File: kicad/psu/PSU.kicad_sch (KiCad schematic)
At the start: 56 parts, among them J1 B2B-PH-K-S, J2 Conn_01x09_Pin, J3 *, U1 BQ21040DBVR, U2 RT4812GJ8F, U3 AP3445LW6-7, U4 AP3445LW6-7

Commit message: Minor PSU changes
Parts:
- added U5: LM66200DRLR, SOT-5X3_DRL_TEX, symbol 2025-12-15_03-55-30:LM66200DRLR
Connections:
- net GND: now also U5.1 (GND), U5.4 (ON), U5.5 (GND)
- net Vcharger: now also U5.2 (VOUT), U5.7 (VOUT); no longer D5.1 (K), J3.A9 (VBUS), J3.B9 (VBUS)
- new net Vcharger_MCU: D5.1 (K), U5.6 (VIN2)
- new net Vcharger_USB: J3.A9 (VBUS), J3.B9 (VBUS), U5.3 (VIN1), U5.8 (ST)

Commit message: PSU Diodes
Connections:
- net 3.3V: now also D4.2 (A)
- net 3.3V_T: no longer D4.2 (A)
- net Vcharger_USB: no longer U5.8 (ST)
- no-connect marks 0 -> 1
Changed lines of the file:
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@@
 		(color 0 0 0 0)
+	)
+	(no_connect
+		(at 154.94 181.61)
 	)
 	(wire
@@
 		)
 	)
-	(global_label "3.3V_T"
+	(global_label "3.3V"
 		(shape input)
 		(at 68.58 31.75 180)
@@
 		)
 		(property "Intersheetrefs" "${INTERSHEET_REFS}"
-			(at 59.5472 31.75 0)
+			(at 61.4824 31.75 0)
 			(effects
 				(font
@@
 				(hide yes)
 			)
-		)
-	)
-	(global_label "Vcharger_USB"
-		(shape input)
-		(at 154.94 181.61 0)
-		(fields_autoplaced yes)
-		(effects
-			(font
-				(size 1.27 1.27)
-			)
-			(justify left)
-		)
-		(property "Intersheetrefs" "${INTERSHEET_REFS}"
-			(at 170.988 181.61 0)
-			(effects
-				(font
-					(size 1.27 1.27)
-				)
-				(justify left)
-				(hide yes)
-			)

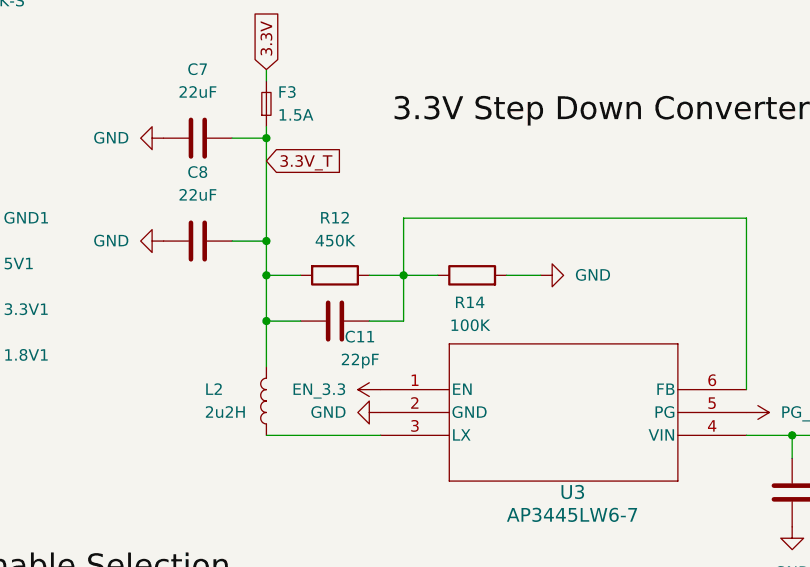
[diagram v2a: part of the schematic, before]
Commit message: Minor PSU Tweaks
removed non existent resistors and updated components
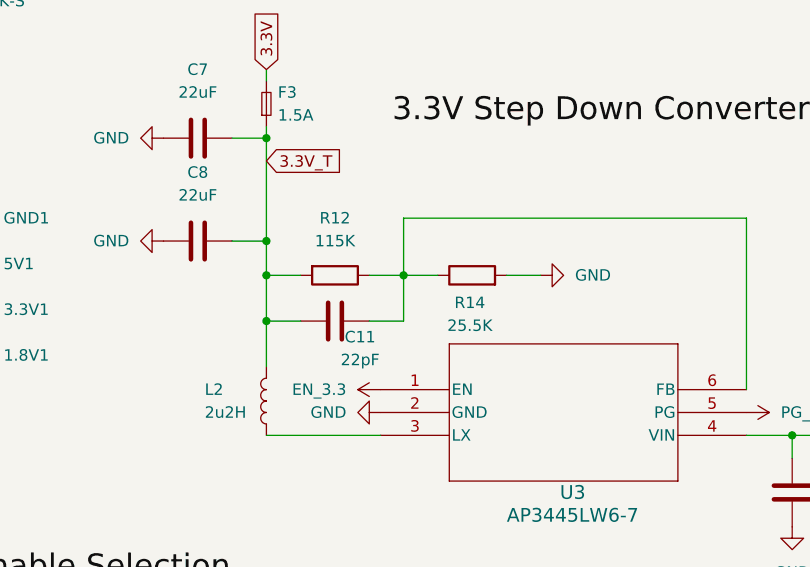
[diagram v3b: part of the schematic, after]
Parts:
- D2, D3, D4, D5, D6: footprint Diode_SMD:D_0805_2012Metric -> Diode_SMD:D_SOD-123
- F2, F3, F4: footprint Fuse:Fuse_0805_2012Metric -> Fuses:0451Series_LTF
- R12: value 450K -> 115K
- R14: value 100K -> 25.5K
- U5: footprint SOT-5X3_DRL_TEX -> footprints:SOT-5X3_DRL_TEX
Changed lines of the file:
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@@
 			)
 		)
-		(property "Value" "450K"
+		(property "Value" "115K"
 			(at 195.58 102.87 90)
 			(effects
@@
 			)
 		)
-		(property "Footprint" "Diode_SMD:D_0805_2012Metric"
+		(property "Footprint" "Diode_SMD:D_SOD-123"
 			(at 72.39 26.67 0)
 			(effects
@@
 			)
 		)
-		(property "Footprint" "Diode_SMD:D_0805_2012Metric"
+		(property "Footprint" "Diode_SMD:D_SOD-123"
 			(at 72.39 31.75 0)
 			(effects
@@
 			)
 		)
-		(property "Footprint" "Diode_SMD:D_0805_2012Metric"
+		(property "Footprint" "Diode_SMD:D_SOD-123"
 			(at 72.39 29.21 0)
 			(effects
@@
 			)
 		)
-		(property "Footprint" "SOT-5X3_DRL_TEX"
+		(property "Footprint" "footprints:SOT-5X3_DRL_TEX"
 			(at 114.3 181.61 0)
 			(effects
@@
 			)
 		)
-		(property "Footprint" "Diode_SMD:D_0805_2012Metric"
+		(property "Footprint" "Diode_SMD:D_SOD-123"
 			(at 71.12 46.99 0)
 			(effects
@@
 			)
 		)
-		(property "Footprint" "Fuse:Fuse_0805_2012Metric"
+		(property "Footprint" "Fuses:0451Series_LTF"
 			(at 190.5 22.86 0)
 			(effects
@@
 			)
 		)
-		(property "Footprint" "Diode_SMD:D_0805_2012Metric"
+		(property "Footprint" "Diode_SMD:D_SOD-123"
 			(at 72.39 34.29 0)
 			(effects
@@
 			)
 		)
-		(property "Value" "100K"
+		(property "Value" "25.5K"
 			(at 210.566 112.268 90)
 			(effects
@@
 			)
 		)
-		(property "Footprint" "Fuse:Fuse_0805_2012Metric"
+		(property "Footprint" "Fuses:0451Series_LTF"
 			(at 127 148.59 0)
 			(effects
@@
 			)
 		)
-		(property "Footprint" "Fuse:Fuse_0805_2012Metric"
+		(property "Footprint" "Fuses:0451Series_LTF"
 			(at 187.96 87.63 0)
 			(effects

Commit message: Update PSU.kicad_sch
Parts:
- R6: value 100K -> 30K
- R7: value 900K -> 270K
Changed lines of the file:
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@@
 			)
 		)
-		(property "Value" "100K"
+		(property "Value" "30K"
 			(at 99.06 154.9399 0)
 			(effects
@@
 			)
 		)
-		(property "Value" "900K"
+		(property "Value" "270K"
 			(at 99.06 165.0999 0)
 			(effects

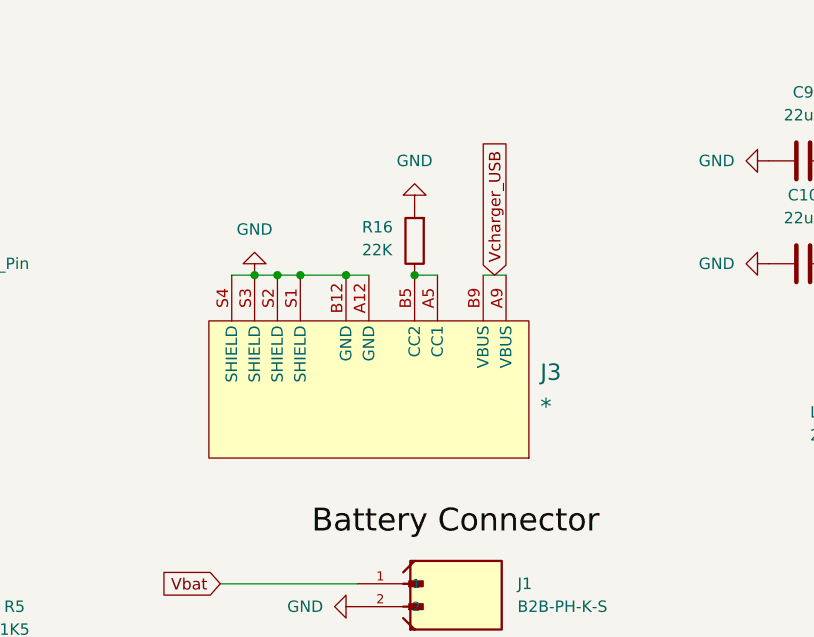
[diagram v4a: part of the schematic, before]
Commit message: new symbols & footprints for connectors and usb-c
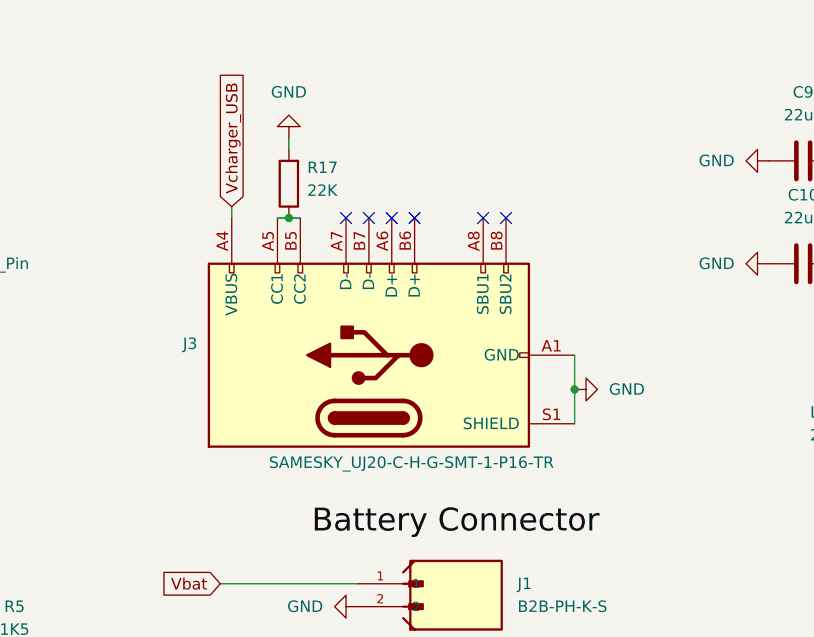
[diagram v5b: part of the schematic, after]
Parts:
- removed J3: *, PSAT_Library:GCT_USB4125-GF-A_REVA2, symbol PSAT_Library:USB4125-GF-A_REVA2
- removed R16: 22K, Resistor_SMD:R_0805_2012Metric, symbol Device:R
- added J3: SAMESKY_UJ20-C-H-G-SMT-1-P16-TR, UJ20_C_H_G_SMT_1_P16_TR:SAMESKY_UJ20-C-H-G-SMT-1-P16-TR, symbol Connector:USB_C_Receptacle_USB2.0_16P
- added R17: 22K, Resistor_SMD:R_0805_2012Metric, symbol Device:R
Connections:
- net GND: now also J3.A1 (GND), J3.A12 (GND), J3.B1 (GND), J3.B12 (GND), J3.S1 (SHIELD), R17.2
- net Vcharger_USB: now also J3.A4 (VBUS), J3.A9 (VBUS), J3.B4 (VBUS), J3.B9 (VBUS)
- new net: J3.A5 (CC1), J3.B5 (CC2), R17.1
- no-connect marks 1 -> 7

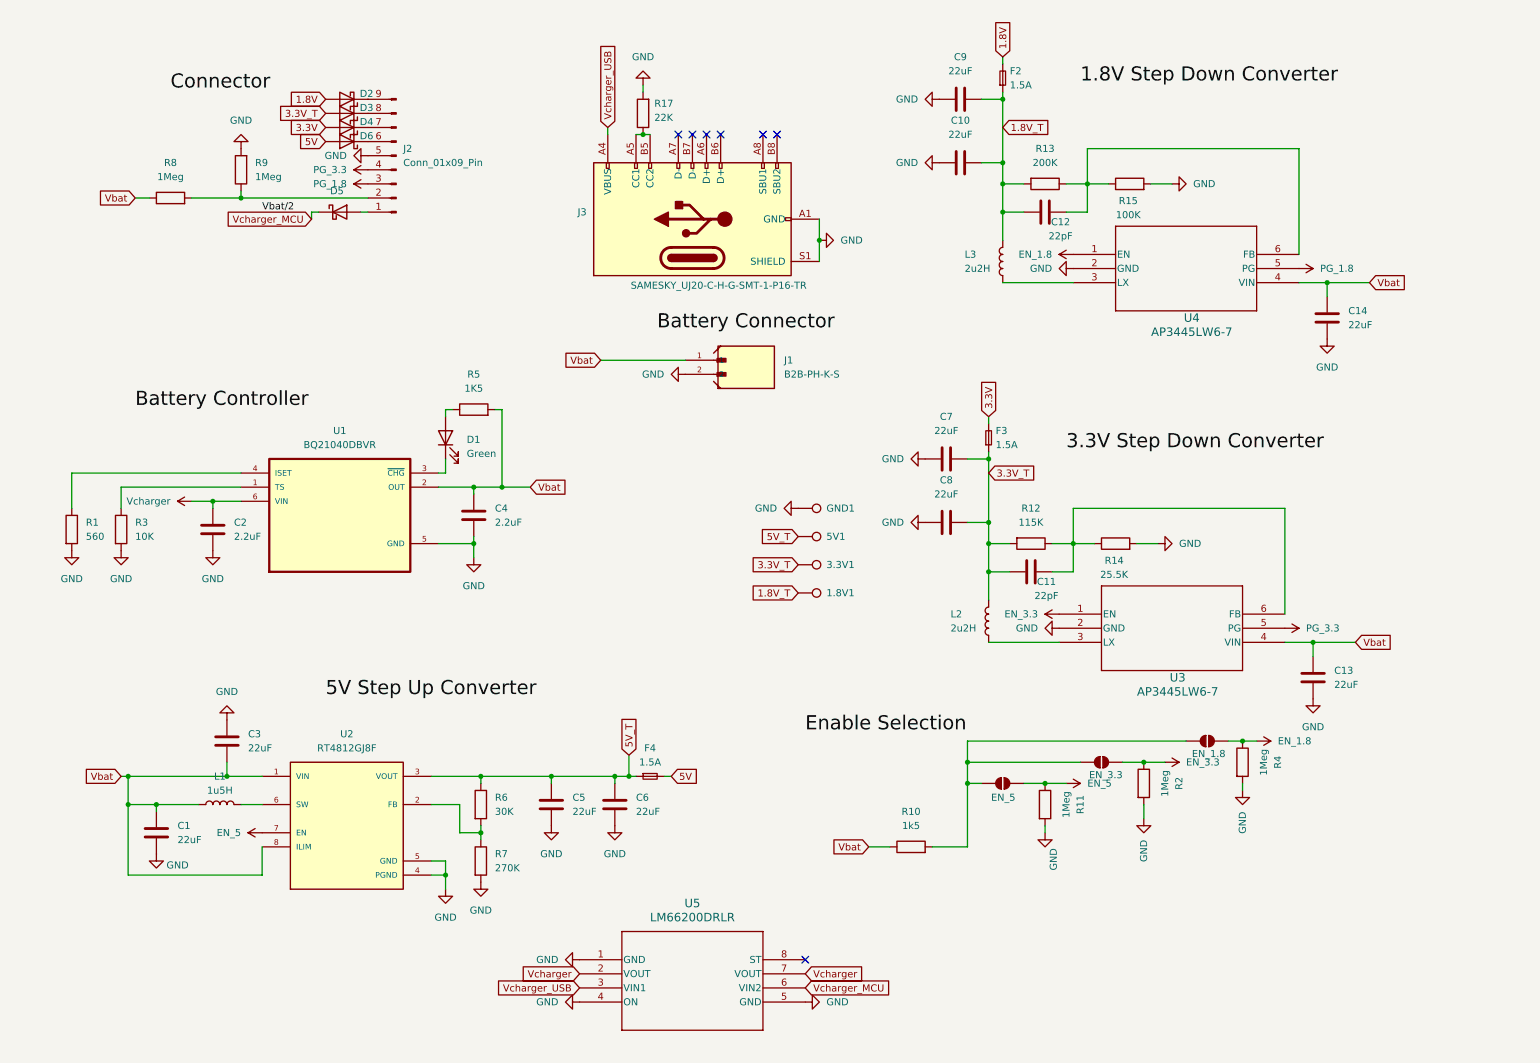
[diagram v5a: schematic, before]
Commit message: Kicad(psu): changed the connector and usb-c to different psu footprints
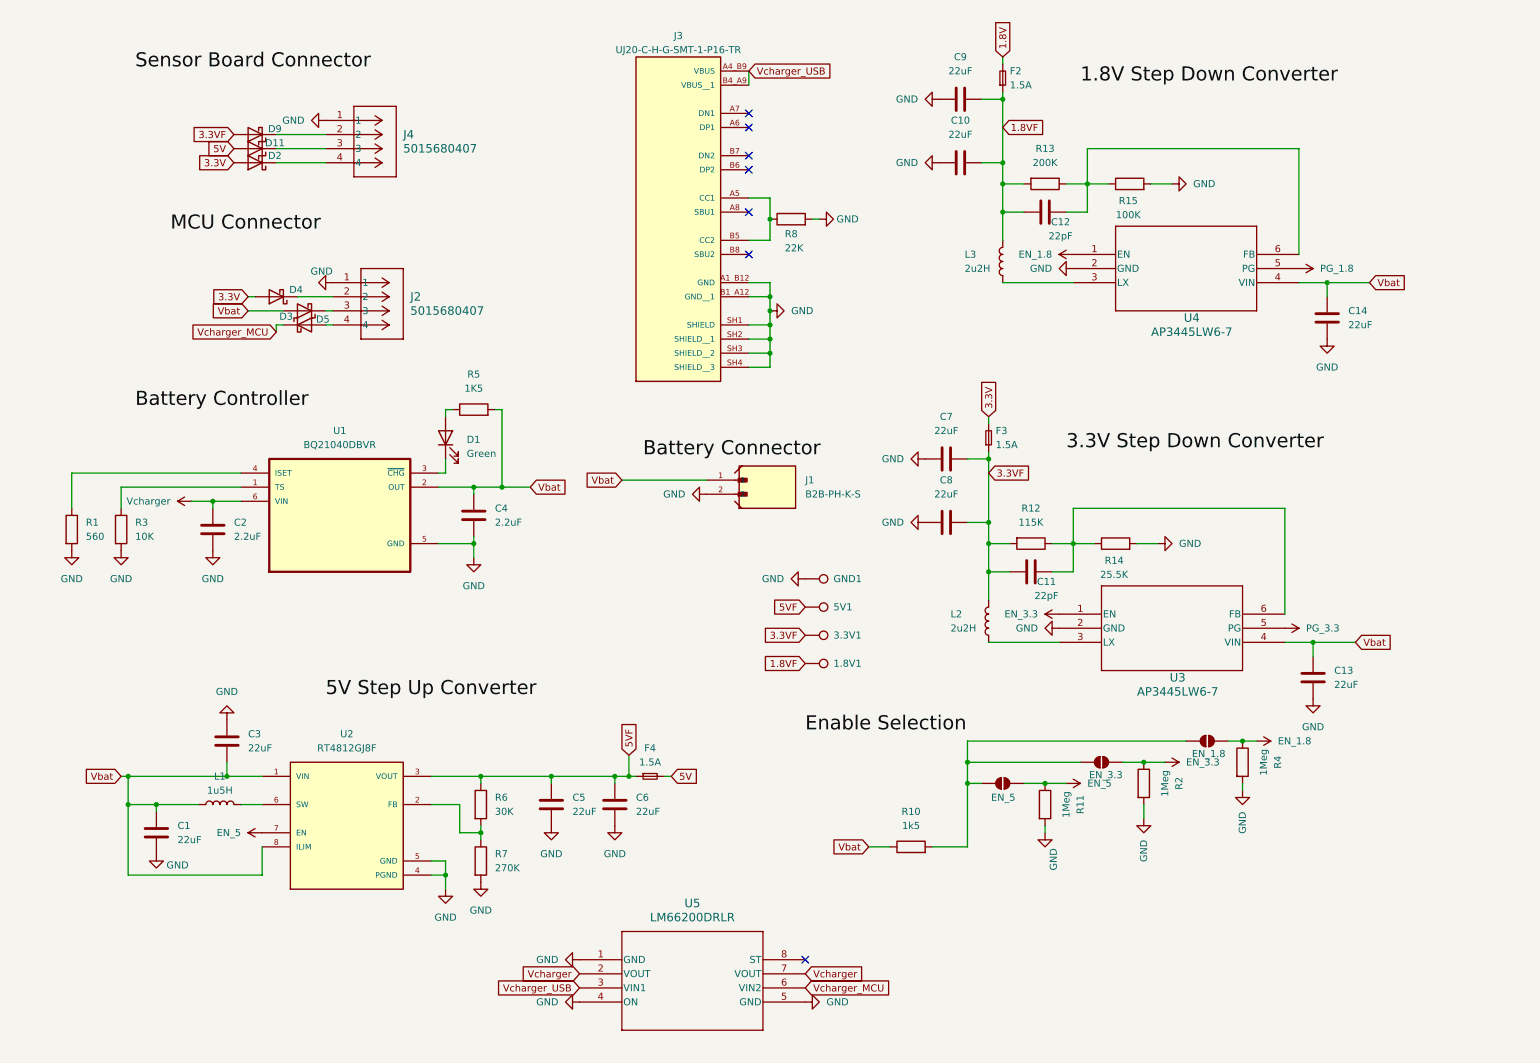
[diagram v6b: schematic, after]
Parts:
- removed D6: D_Schottky, Diode_SMD:D_SOD-123, symbol Device:D_Schottky
- removed J2: Conn_01x09_Pin, Connector_PinSocket_2.54mm:PinSocket_1x09_P2.54mm_Vertical, symbol Connector:Conn_01x09_Pin
- removed J3: SAMESKY_UJ20-C-H-G-SMT-1-P16-TR, UJ20_C_H_G_SMT_1_P16_TR:SAMESKY_UJ20-C-H-G-SMT-1-P16-TR, symbol Connector:USB_C_Receptacle_USB2.0_16P
- removed R17: 22K, Resistor_SMD:R_0805_2012Metric, symbol Device:R
- removed R9: 1Meg, Resistor_SMD:R_0805_2012Metric, symbol Device:R
- added D11, D9: D_Schottky, Diode_SMD:D_SOD-123, symbol Device:D_Schottky
- added J2, J4: 5015680407, CONN_5015680000-SD_04_MOL, symbol 2026-01-26_05-30-52:5015680407
- added J3: UJ20-C-H-G-SMT-1-P16-TR, SAMESKY_UJ20-C-H-G-SMT-1-P16-TR, symbol UJ20-C-H-G-SMT-1-P16-TR:UJ20-C-H-G-SMT-1-P16-TR
- R8: value 1Meg -> 22K
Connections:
- net 1.8V: no longer D2.2 (A)
- net 3.3V: now also D2.2 (A)
- net 5V: now also D11.2 (A)
- net GND: now also R8.2, J2.1, J3.A1_B12 (GND), J3.B1_A12 (GND__1), J3.SH1 (SHIELD), J3.SH2 (SHIELD__1), J3.SH3 (SHIELD__2), J3.SH4 (SHIELD__3), J4.1
- net Vbat: now also D3.2 (A); no longer R8.1
- net Vcharger_USB: now also J3.A4_B9 (VBUS), J3.B4_A9 (VBUS__1)
- net at D2.1 (K): now also J4.4
- net at D4.1 (K): now also J2.2
- net at D3.1 (K): now also J2.3
- net at D5.2 (A): now also J2.4
- net 1.8V_T renamed 1.8VF
- net 3.3V_T renamed 3.3VF
- net 3.3VF: now also D9.2 (A); no longer D3.2 (A)
- net 5V_T renamed 5VF
- new net: D9.1 (K), J4.2
- new net: D11.1 (K), J4.3
- new net: J3.A5 (CC1), J3.B5 (CC2), R8.1
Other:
- moved on the sheet: 1.8V1, 3.3V1, 5V1, D4, D5, GND1, J1
